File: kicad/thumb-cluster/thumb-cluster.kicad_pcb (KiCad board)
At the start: 2 copper layers, 21 x 45 mm, 15 parts, among them J4 59453-081110EDHLF

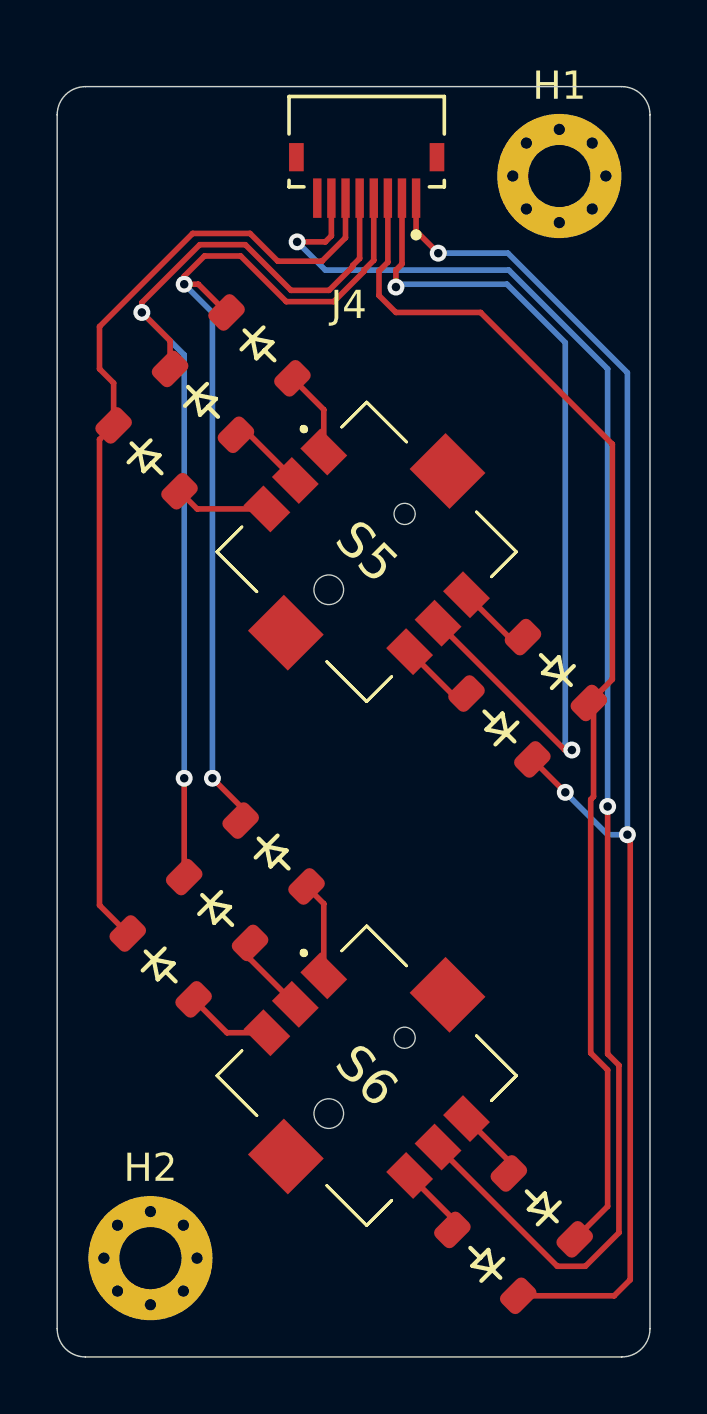
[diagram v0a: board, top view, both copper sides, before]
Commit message: update thumb cluster
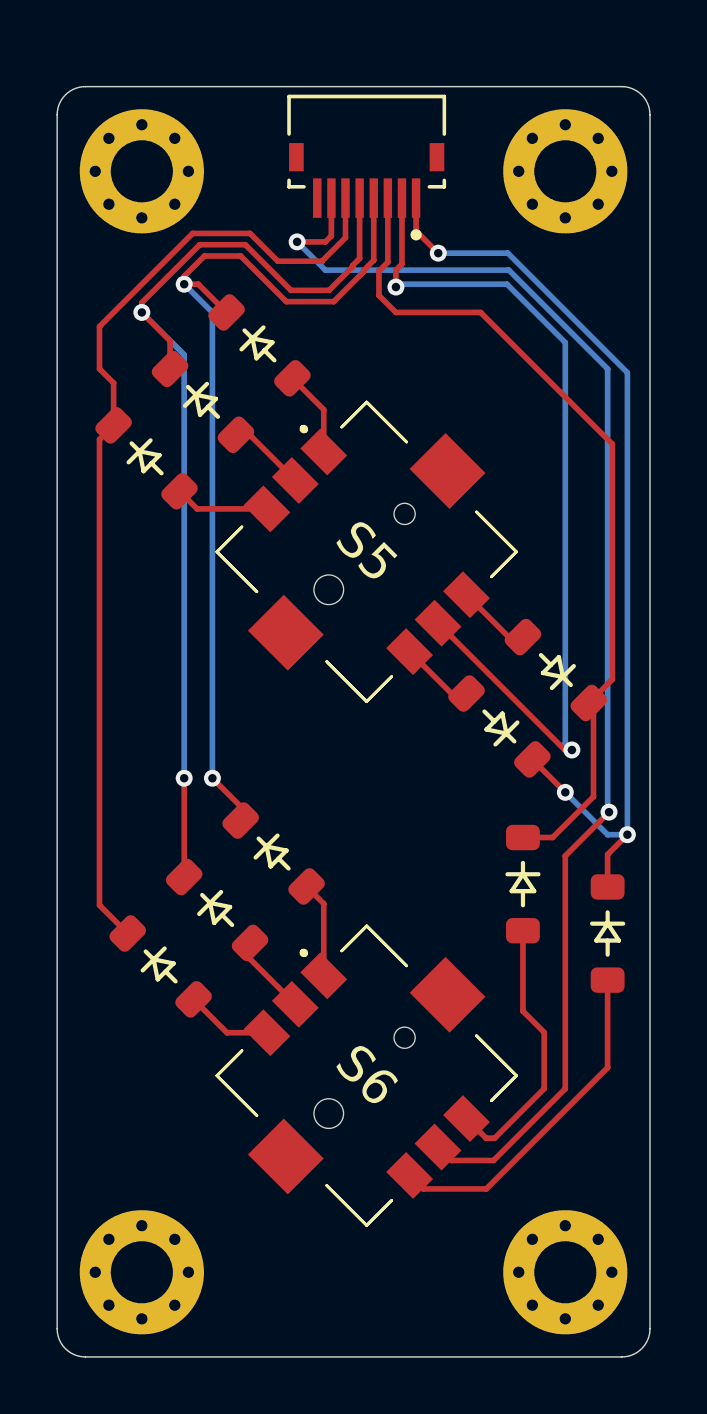
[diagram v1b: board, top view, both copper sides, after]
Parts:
- added H3: Mounting_Hole, footprints:MountingHole_2.2mm_M2_Pad_Via, F.Cu at (37.5, 66.0)
- added H4: Mounting_Hole, footprints:MountingHole_2.2mm_M2_Pad_Via, F.Cu at (22.5, 27.0)
- H1, H2: footprint MountingHole:MountingHole_2.2mm_M2_Pad_Via -> footprints:MountingHole_2.2mm_M2_Pad_Via
- moved D30 12.4 mm to (39.0, 54.0), turned to -90 degrees
- moved D29 11.4 mm to (36.0, 52.2), turned to -90 degrees
- moved H2 0.59 mm to (22.5, 66.0)
- moved H1 0.27 mm to (37.5, 27.0)
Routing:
- net ERow 5: track 51.6 -> 33.8 mm
- net ERow 4: track 43.4 -> 30.0 mm
- net Net-(D30-A): track 2.56 -> 12.1 mm
- net ECol 6: track 54.9 -> 47.4 mm
- net Net-(D29-A): track 2.57 -> 9.67 mm

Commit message: update
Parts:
- moved D30 1.57 mm to (39.2, 52.5)
- moved D29 0.20 mm to (36.0, 52.5)
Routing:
- net ERow 5: track 33.8 -> 31.7 mm
- net Net-(D30-A): track 12.1 -> 13.8 mm
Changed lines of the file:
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@@
 	(footprint "ScottoKeebs_Components:Diode_SOD-123"
 		(layer "F.Cu")
-		(at 39 54 -90)
+		(at 39.25 52.45 -90)
 		(descr "SOD-123")
 		(tags "SOD-123")
@@
 	(footprint "ScottoKeebs_Components:Diode_SOD-123"
 		(layer "F.Cu")
-		(at 36 52.25 -90)
+		(at 36 52.45 -90)
 		(descr "SOD-123")
 		(tags "SOD-123")
@@
 	)
 	(segment
-		(start 31.5 32)
-		(end 34.5 32)
+		(start 36.65 49.6)
+		(end 37.748529 49.6)
 		(width 0.2)
 		(layer "F.Cu")
@@
 	)
 	(segment
-		(start 34.5 32)
-		(end 39.166904 36.666904)
+		(start 31.5 32)
+		(end 34.5 32)
 		(width 0.2)
 		(layer "F.Cu")
@@
 	)
 	(segment
-		(start 36 50.6)
-		(end 37.051471 50.6)
+		(start 34.5 32)
+		(end 39.166904 36.666904)
 		(width 0.2)
 		(layer "F.Cu")
@@
 	)
 	(segment
-		(start 38.5 46)
-		(end 38.333452 45.833452)
+		(start 36 50.8)
+		(end 36 50.25)
 		(width 0.2)
 		(layer "F.Cu")
@@
 	)
 	(segment
-		(start 37.051471 50.6)
-		(end 38.5 49.151471)
+		(start 37.748529 49.6)
+		(end 38.333452 49.015077)
 		(width 0.2)
 		(layer "F.Cu")
@@
 	)
 	(segment
-		(start 38.5 49.151471)
-		(end 38.5 46)
+		(start 31.214466 30.219848)
+		(end 30.9 30.534314)
 		(width 0.2)
 		(layer "F.Cu")
@@
 	)
 	(segment
-		(start 31.214466 30.219848)
-		(end 30.9 30.534314)
+		(start 30.9 30.534314)
+		(end 30.9 31.4)
 		(width 0.2)
 		(layer "F.Cu")
@@
 	)
 	(segment
-		(start 30.9 30.534314)
-		(end 30.9 31.4)
+		(start 36 50.25)
+		(end 36.65 49.6)
 		(width 0.2)
 		(layer "F.Cu")
@@
 	)
 	(segment
-		(start 33 29.9)
-		(end 32.214466 29.114466)
+		(start 38.333452 49.015077)
+		(end 38.333452 45.833452)
 		(width 0.2)
 		(layer "F.Cu")
-		(net 9)
+		(net 8)
 	)
 	(segment
-		(start 32.214466 29.114466)
-		(end 32.214466 27.95)
+		(start 33 29.9)
+		(end 32.214466 29.114466)
 		(width 0.2)
 		(layer "F.Cu")
@@
 	)
 	(segment
-		(start 39.8 50.6)
-		(end 39.7 50.5)
+		(start 32.214466 29.114466)
+		(end 32.214466 27.95)
 		(width 0.2)
 		(layer "F.Cu")
@@
 	)
 	(segment
-		(start 39 52.35)
-		(end 39 51.2)
+		(start 39.25 50.8)
+		(end 39.7 50.35)
 		(width 0.2)
 		(layer "F.Cu")
@@
 	)
 	(segment
-		(start 39 51.2)
-		(end 39.7 50.5)
+		(start 39.7 50.35)
+		(end 39.7 48.25)
 		(width 0.2)
 		(layer "F.Cu")
@@
 	)
 	(via
-		(at 39.7 50.5)
+		(at 39.7 48.25)
 		(size 0.6)
 		(drill 0.3)
@@
 	)
 	(segment
-		(start 39 50.5)
-		(end 37.5 49)
+		(start 39.7 48.25)
+		(end 39.7 34.134314)
 		(width 0.2)
 		(layer "B.Cu")
@@
 	)
 	(segment
-		(start 39.7 50.5)
-		(end 39 50.5)
+		(start 38.95 49)
+		(end 37.5 49)
 		(width 0.2)
 		(layer "B.Cu")
@@
 	)
 	(segment
-		(start 39.7 50.5)
-		(end 39.7 34.134314)
+		(start 39.7 48.25)
+		(end 38.95 49)
 		(width 0.2)
 		(layer "B.Cu")
@@
 	(segment
 		(start 36 56.75)
-		(end 36 53.9)
+		(end 36 54.1)
 		(width 0.2)
 		(layer "F.Cu")
@@
 	)
 	(segment
-		(start 31.984746 62.571068)
-		(end 32.462043 63.048365)
+		(start 39.3 54.15)
+		(end 39.25 54.1)
 		(width 0.2)
 		(layer "F.Cu")
@@
 	)
 	(segment
-		(start 32.462043 63.048365)
-		(end 34.701635 63.048365)
+		(start 39.3 58.45)
+		(end 39.3 54.15)
+		(width 0.2)
+		(layer "F.Cu")
+		(net 18)
+	)
+	(segment
+		(start 31.984746 62.571068)
+		(end 32.462043 63.048365)
 		(width 0.2)
 		(layer "F.Cu")
@@
 	(segment
 		(start 34.701635 63.048365)
-		(end 39 58.75)
+		(end 39.3 58.45)
 		(width 0.2)
 		(layer "F.Cu")
@@
 	)
 	(segment
-		(start 39 58.75)
-		(end 39 55.65)
+		(start 32.462043 63.048365)
+		(end 34.701635 63.048365)
 		(width 0.2)
 		(layer "F.Cu")
@@
 	)
 	(segment
-		(start 33.46967 62.040738)
-		(end 32.992373 61.563441)
+		(start 37.5 59.5)
+		(end 34.959262 62.040738)
 		(width 0.2)
 		(layer "F.Cu")
@@
 	)
 	(segment
-		(start 39.049265 49.700735)
-		(end 37.5 51.25)
+		(start 37.914214 50)
+		(end 37.5 50)
+		(width 0.2)
+		(layer "F.Cu")
+		(net 22)
+	)
+	(segment
+		(start 38.9 47.7)
+		(end 38.9 49.014214)
 		(width 0.2)
 		(layer "F.Cu")
@@
 	)
 	(segment
+		(start 34.959262 62.040738)
+		(end 33.46967 62.040738)
+		(width 0.2)
+		(layer "F.Cu")
+		(net 22)
+	)
+	(segment
 		(start 28 29.5)
 		(end 29 29.5)
@@
 	)
 	(segment
-		(start 37.5 51.25)
+		(start 37.5 50)
 		(end 37.5 59.5)
 		(width 0.2)
@@
 	)
 	(segment
-		(start 37.5 59.5)
-		(end 34.959262 62.040738)
+		(start 39.1 47.5)
+		(end 38.9 47.7)
 		(width 0.2)
 		(layer "F.Cu")
@@
 	)
 	(segment
-		(start 34.959262 62.040738)
-		(end 33.46967 62.040738)
+		(start 38.9 49.014214)
+		(end 37.914214 50)
+		(width 0.2)
+		(layer "F.Cu")
+		(net 22)
+	)
+	(segment
+		(start 33.46967 62.040738)
+		(end 32.992373 61.563441)
 		(width 0.2)
 		(layer "F.Cu")
@@
 	)
 	(via
-		(at 39.049265 49.700735)
+		(at 39.1 47.5)
 		(size 0.6)
 		(drill 0.3)
@@
 	)
 	(segment
-		(start 39.049265 49.700735)
-		(end 39 49.65147)
+		(start 35.5 30.5)
+		(end 29 30.5)
 		(width 0.2)
 		(layer "B.Cu")
@@
 	)
 	(segment
-		(start 39 34)
-		(end 35.5 30.5)
+		(start 39 47.4)
+		(end 39 34)
 		(width 0.2)
 		(layer "B.Cu")
@@
 	)
 	(segment
-		(start 39 49.65147)
-		(end 39 34)
+		(start 39.1 47.5)
+		(end 39 47.4)
 		(width 0.2)
 		(layer "B.Cu")
@@
 	)
 	(segment
-		(start 35.5 30.5)
-		(end 29 30.5)
+		(start 39 34)
+		(end 35.5 30.5)
 		(width 0.2)
 		(layer "B.Cu")
